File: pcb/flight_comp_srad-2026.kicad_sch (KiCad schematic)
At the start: 75 parts, among them J1 503398-1892, J2 Connector_3, J3 USB_B_Micro, J5 Vin_Bat, U1 IIM-20670, U3 RP2040, U4 ADXL375BCCZ-RL7, U5 MAX-M10M-00B, U6 W25Q128JVS, U7 XBP9B-DMSTB002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

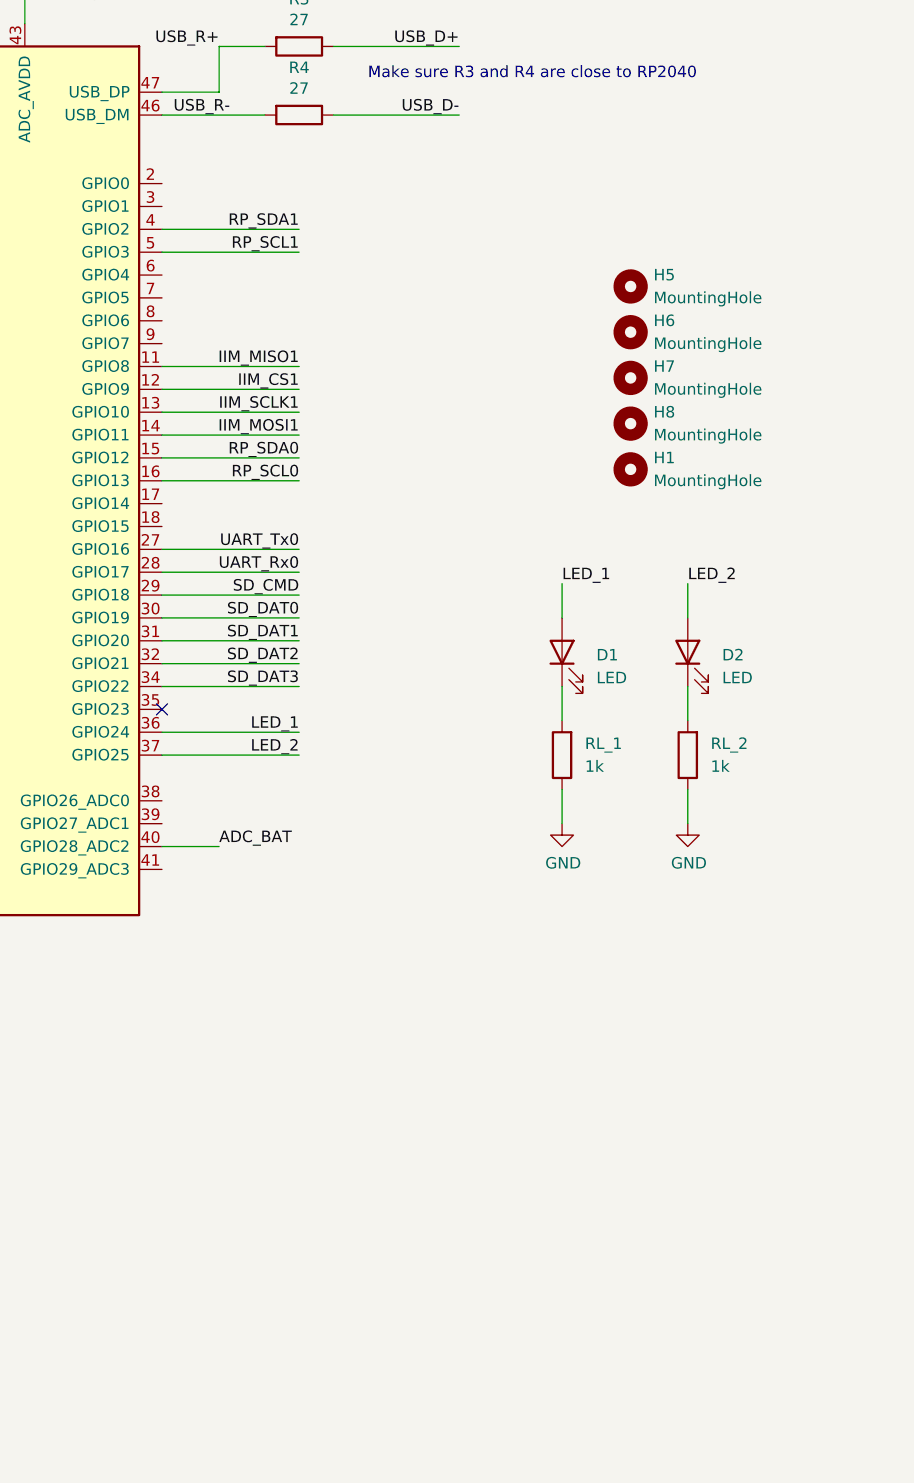
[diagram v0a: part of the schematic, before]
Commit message: Adición buzzer y corrección de algunos errores
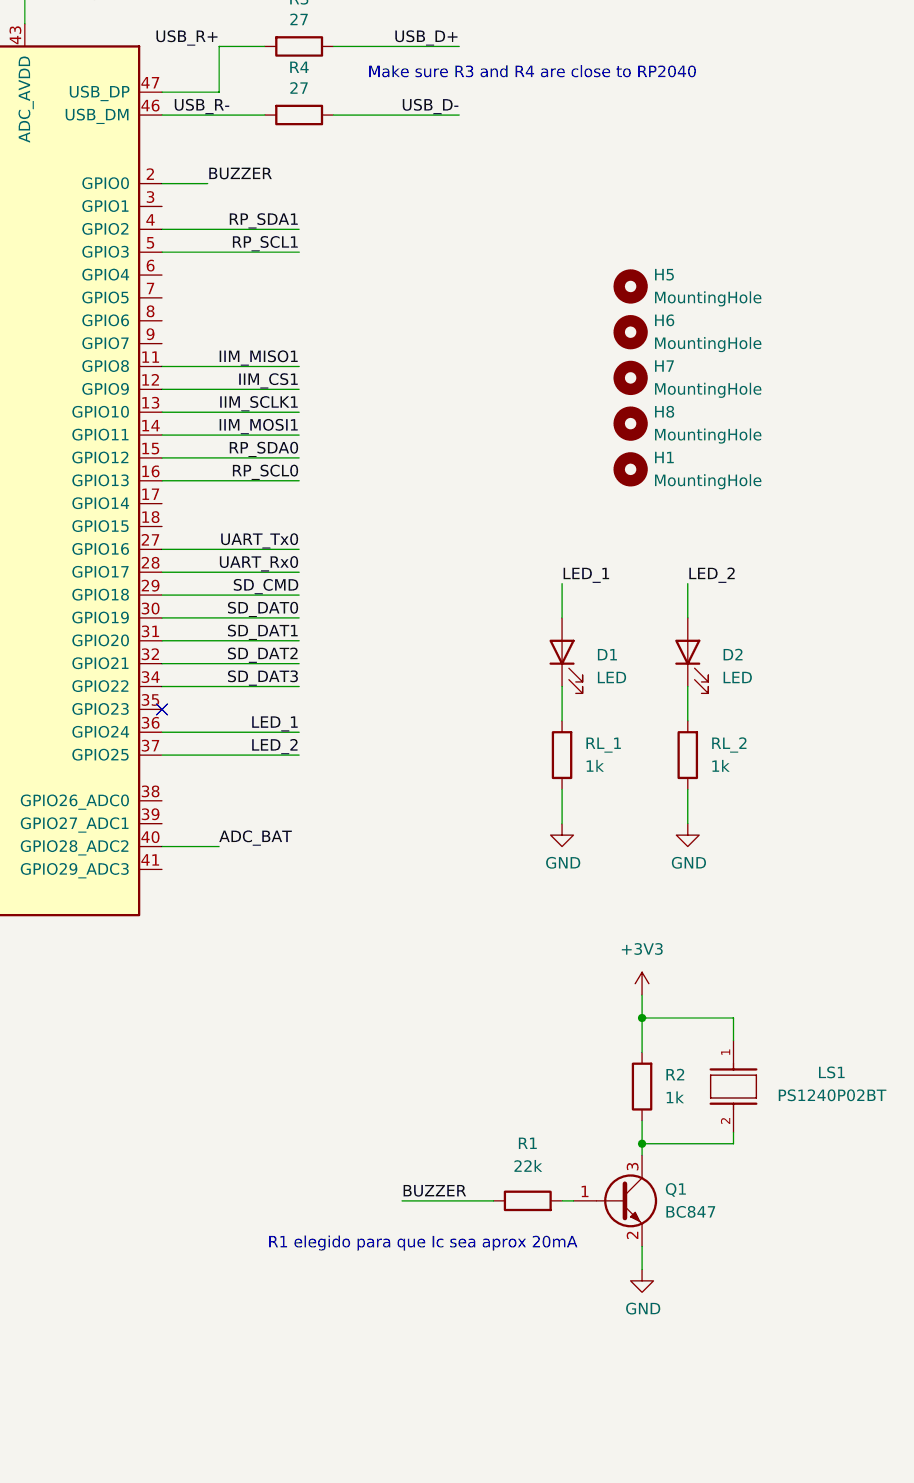
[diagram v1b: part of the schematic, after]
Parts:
- added LS1: PS1240P02BT, Buzzer_Beeper:Buzzer_TDK_PS1240P02BT_D12.2mm_H6.5mm, symbol PS1240P02BT:PS1240P02BT
- added Q1: BC847, Package_TO_SOT_SMD:SOT-23, symbol Transistor_BJT:BC847
- added R1: 22k, Resistor_SMD:R_0805_2012Metric, symbol Device:R
- added R2: 1k, Resistor_SMD:R_0805_2012Metric, symbol Device:R
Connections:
- net +3V3: now also LS1.1, R2.2
- net GND: now also Q1.2 (E)
- net BUZZER: now reaches U3.2 (GPIO0)
- net BUZZER: now also R1.1
- new net: Q1.1 (B), R1.2
- new net: LS1.2, Q1.3 (C), R2.1
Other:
- note added: "R1 elegido para que Ic sea aprox 20mA"

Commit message: quedan 5 errores
creo que todos los errores son inevitables por el diseño. quedan cosas tipo ancho del texto, pero debería salir bien todo lo importante en JLC
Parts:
- R3, R4: footprint Capacitor_SMD:C_0201_0603Metric -> Resistor_SMD:R_0603_1608Metric
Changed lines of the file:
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@@
 			)
 		)
-		(property "Footprint" "Capacitor_SMD:C_0201_0603Metric"
+		(property "Footprint" "Resistor_SMD:R_0603_1608Metric"
 			(at 500.38 151.892 90)
 			(effects
@@
 			)
 		)
-		(property "Footprint" "Capacitor_SMD:C_0201_0603Metric"
+		(property "Footprint" "Resistor_SMD:R_0603_1608Metric"
 			(at 500.38 159.512 90)
 			(effects
@@
 		(dnp no)
 		(fields_autoplaced yes)
-		(property "Reference" "#PWR034"
+		(property "Reference" "#PWR0101"
 			(at 538.48 262.89 0)
 			(effects
@@
 			(project "flight_comp_srad-2026"
 				(path "/142d7a80-3dfb-4605-bdd8-7dd9e7ca17c7"
-					(reference "#PWR034")
+					(reference "#PWR0101")
 					(unit 1)
 				)

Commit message: srad versión final ahora sí 2.0 intento 17
nigga
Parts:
- J2: footprint TCLib:PinHeader_1x03_P2.54mm_Vertical -> Connector_PinHeader_2.54mm:PinHeader_1x03_P2.54mm_Vertical
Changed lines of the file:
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@@
 			)
 		)
-		(property "Footprint" "TCLib:PinHeader_1x03_P2.54mm_Vertical"
+		(property "Footprint" "Connector_PinHeader_2.54mm:PinHeader_1x03_P2.54mm_Vertical"
 			(at 297.434 257.302 0)
 			(effects

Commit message: PARECE terminado
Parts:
- removed CGPS_3: 100n, Capacitor_SMD:C_0402_1005Metric, symbol Device:C
- added RSPI_1, RSPI_2, RSPI_3, RSPI_4: 1k, Resistor_SMD:R_0603_1608Metric, symbol Device:R
- added TP1, TP2: TestPoint, TestPoint:TestPoint_Pad_D1.0mm, symbol Connector:TestPoint
- CGPS_1: value 100n -> 1u; footprint Capacitor_SMD:C_0402_1005Metric -> Capacitor_SMD:C_0805_2012Metric
- CGPS_2: footprint Capacitor_SMD:C_0402_1005Metric -> Capacitor_SMD:C_0603_1608Metric
- CTX1, R8, RFLASH_1: now not fitted
- CXB_1, CXB_2: footprint Capacitor_SMD:C_0603_1608Metric -> Capacitor_SMD:C_0805_2012Metric
- D1: value LED -> LED_B
- D2: value LED -> LED_R
- RI2C_1, RI2C_2: value 10k -> 1k; footprint Resistor_SMD:R_0402_1005Metric -> Resistor_SMD:R_0603_1608Metric
- RI2C_3, RI2C_4: value 10k -> 1k; footprint Resistor_SMD:R_0805_2012Metric -> Resistor_SMD:R_0603_1608Metric
- RL_1: value 1k -> 39
- RL_2: value 1k -> 150
- U1: footprint Package_DFN_QFN:QFN-24-1EP_5x5mm_P0.65mm_EP3.25x3.25mm -> SRAD:QFN50P450X450X115-25N
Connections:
- net +3V3: now also RSPI_1.2, RSPI_2.2, RSPI_3.2, RSPI_4.2, TP1.1
- net GND: now also TP2.1
- net IIM_CS1: now also RSPI_4.1
- net IIM_MISO1: now also RSPI_1.1
- net IIM_MOSI1: now also RSPI_2.1
- net IIM_SCLK1: now also RSPI_3.1
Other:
- moved on the sheet: CIIM_1, CIIM_2, CIIM_3, CIIM_4, U1

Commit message: version final?
uwu
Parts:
- added TP3: TestPoint, TestPoint:TestPoint_Pad_D1.0mm, symbol Connector:TestPoint
- Div_res_bat1, Div_res_bat2: now not fitted
- RSPI_4: value 1k -> 10k
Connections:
- net +1V1: now also TP3.1
- no-connect marks 33 -> 43
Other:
- note added: "3V3?"
- moved on the sheet: TP2
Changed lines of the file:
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@@
 		)
 	)
+	(text "3V3?"
+		(exclude_from_sim no)
+		(at 144.272 61.722 0)
+		(effects
+			(font
+				(size 1.27 1.27)
+			)
+		)
+	)
 	(text "JLC04161H-7628E\nW=0.7\nGap=0.4\nThickness=0.4284 mm"
 		(exclude_from_sim no)
@@
 	)
 	(junction
+		(at 412.75 118.11)
+		(diameter 0)
+		(color 0 0 0 0)
+	)
+	(junction
 		(at 513.08 129.54)
 		(diameter 0)
@@
 	)
 	(no_connect
+		(at 485.14 186.69)
+	)
+	(no_connect
 		(at 48.26 50.8)
 	)
@@
 	)
 	(no_connect
+		(at 485.14 240.03)
+	)
+	(no_connect
+		(at 485.14 171.45)
+	)
+	(no_connect
 		(at 100.33 137.16)
 	)
 	(no_connect
+		(at 485.14 237.49)
+	)
+	(no_connect
 		(at 100.33 116.84)
 	)
@@
 	)
 	(no_connect
+		(at 485.14 184.15)
+	)
+	(no_connect
 		(at 306.07 130.81)
 	)
@@
 	)
 	(no_connect
+		(at 485.14 204.47)
+	)
+	(no_connect
 		(at 190.5 344.17)
 	)
@@
 	)
 	(no_connect
+		(at 485.14 179.07)
+	)
+	(no_connect
 		(at 190.5 331.47)
 	)
@@
 	)
 	(no_connect
+		(at 485.14 207.01)
+	)
+	(no_connect
+		(at 485.14 181.61)
+	)
+	(no_connect
 		(at 190.5 346.71)
 	)
@@
 		(at 190.5 361.95)
 	)
+	(no_connect
+		(at 485.14 245.11)
+	)
 	(wire
 		(pts
@@
 	(wire
 		(pts
-			(xy 485.14 168.91) (xy 490.22 168.91)
+			(xy 485.14 168.91) (xy 500.38 168.91)
 		)
 		(stroke
@@
 	(wire
 		(pts
+			(xy 412.75 115.57) (xy 412.75 118.11)
+		)
+		(stroke
+			(width 0)
+			(type default)
+		)
+	)
+	(wire
+		(pts
 			(xy 52.07 252.73) (xy 52.07 250.19)
 		)
@@
 	)
 	(label "BUZZER"
-		(at 490.22 168.91 0)
+		(at 500.38 168.91 180)
 		(effects
 			(font
 				(size 1.27 1.27)
 			)
-			(justify left bottom)
+			(justify right bottom)
 		)
 	)
@@
 			)
 		)
-		(property "Value" "1k"
+		(property "Value" "10k"
 			(at 52.832 330.454 90)
 			(effects
@@
 		(lib_name "GND_12")
 		(lib_id "power:GND")
-		(at 501.65 87.63 0)
+		(at 563.88 129.54 0)
 		(unit 1)
 		(exclude_from_sim no)
@@
 		(dnp no)
 		(property "Reference" "#PWR038"
-			(at 501.65 93.98 0)
+			(at 563.88 135.89 0)
 			(effects
 				(font
@@
 		)
 		(property "Value" "GND"
-			(at 501.777 92.0242 0)
+			(at 564.007 133.9342 0)
 			(effects
 				(font
@@
 		)
 		(property "Footprint" ""
-			(at 501.65 87.63 0)
+			(at 563.88 129.54 0)
 			(effects
 				(font
@@
 		)
 		(property "Datasheet" ""
-			(at 501.65 87.63 0)
+			(at 563.88 129.54 0)
 			(effects
 				(font
@@
 		)
 		(property "Description" ""
-			(at 501.65 87.63 0)
+			(at 563.88 129.54 0)
 			(effects
 				(font
@@
 		(in_bom yes)
 		(on_board yes)
-		(dnp no)
+		(dnp yes)
 		(property "Reference" "Div_res_bat2"
 			(at 76.2 72.39 0)
@@
 	(symbol
 		(lib_id "Connector:TestPoint")
-		(at 501.65 87.63 0)
+		(at 563.88 129.54 0)
 		(unit 1)
 		(exclude_from_sim no)
@@
 		(fields_autoplaced yes)
 		(property "Reference" "TP2"
-			(at 504.19 83.0579 0)
+			(at 566.42 124.9679 0)
 			(effects
 				(font
@@
 		)
 		(property "Value" "TestPoint"
-			(at 504.19 85.5979 0)
+			(at 566.42 127.5079 0)
 			(effects
 				(font
@@
 		)
 		(property "Footprint" "TestPoint:TestPoint_Pad_D1.0mm"
-			(at 506.73 87.63 0)
+			(at 568.96 129.54 0)
 			(effects
 				(font
@@
 		)
 		(property "Datasheet" "~"
-			(at 506.73 87.63 0)
+			(at 568.96 129.54 0)
 			(effects
 				(font
@@
 		)
 		(property "Description" "test point"
-			(at 501.65 87.63 0)
+			(at 563.88 129.54 0)
 			(effects
 				(font
@@
 	)
 	(symbol
+		(lib_id "Connector:TestPoint")
+		(at 412.75 115.57 0)
+		(unit 1)
+		(exclude_from_sim no)
+		(in_bom yes)
+		(on_board yes)
+		(dnp no)
+		(fields_autoplaced yes)
+		(property "Reference" "TP3"
+			(at 415.29 110.9979 0)
+			(effects
+				(font
+					(size 1.27 1.27)
+				)
+				(justify left)
+			)
+		)
+		(property "Value" "TestPoint"
+			(at 415.29 113.5379 0)
+			(effects
+				(font
+					(size 1.27 1.27)
+				)
+				(justify left)
+			)
+		)
+		(property "Footprint" "TestPoint:TestPoint_Pad_D1.0mm"
+			(at 417.83 115.57 0)
+			(effects
+				(font
+					(size 1.27 1.27)
+				)
+				(hide yes)
+			)
+		)
+		(property "Datasheet" "~"
+			(at 417.83 115.57 0)
+			(effects
+				(font
+					(size 1.27 1.27)
+				)
+				(hide yes)
+			)
+		)
+		(property "Description" "test point"
+			(at 412.75 115.57 0)
+			(effects
+				(font
+					(size 1.27 1.27)
+				)
+				(hide yes)
+			)
+		)
+		(pin "1"
+		)
+		(instances
+			(project "flight_comp_srad-2026"
+				(path "/142d7a80-3dfb-4605-bdd8-7dd9e7ca17c7"
+					(reference "TP3")
+					(unit 1)
+				)
+			)
+		)
+	)
+	(symbol
 		(lib_id "SRAD:MS561101BA03-50")
 		(at 290.83 130.81 0)
@@
 		(in_bom yes)
 		(on_board yes)
-		(dnp no)
+		(dnp yes)
 		(property "Reference" "Div_res_bat1"
 			(at 67.31 63.754 90)

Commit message: versión final ahora sí
OwO
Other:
- note removed: "I2C / SPI"
- note removed: "I2C / UART"
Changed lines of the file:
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@@
 		)
 	)
-	(text "I2C / UART"
+	(text "I2C"
 		(exclude_from_sim no)
 		(at 38.1 96.266 0)
@@
 		)
 	)
-	(text "I2C / SPI"
+	(text "I2C"
 		(exclude_from_sim no)
 		(at 265.684 98.298 0)

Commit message: https://drive.google.com/drive/folders/1AIpmniXnHx3TK0_vEmsLqZfZEH8VMv5M
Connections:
- net LED_1: now also U3.38 (GPIO26_ADC0); no longer U3.36 (GPIO24)
- net LED_2: now also U3.39 (GPIO27_ADC1); no longer U3.37 (GPIO25)
- net SD_CLK: now also U3.37 (GPIO25)
- no-connect marks 43 -> 41
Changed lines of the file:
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@@
 	)
 	(no_connect
-		(at 485.14 227.33)
-	)
-	(no_connect
 		(at 100.33 127)
 	)
 	(no_connect
-		(at 485.14 240.03)
-	)
-	(no_connect
 		(at 485.14 171.45)
 	)
@@
 	)
 	(no_connect
-		(at 485.14 237.49)
+		(at 485.14 229.87)
 	)
 	(no_connect
@@
 	)
 	(no_connect
+		(at 485.14 227.33)
+	)
+	(no_connect
 		(at 246.38 356.87)
 	)
@@
 	)
 	(no_connect
-		(at 485.14 181.61)
-	)
-	(no_connect
 		(at 190.5 346.71)
 	)
@@
 	(wire
 		(pts
+			(xy 485.14 237.49) (xy 500.38 237.49)
+		)
+		(stroke
+			(width 0)
+			(type default)
+		)
+	)
+	(wire
+		(pts
 			(xy 74.93 38.1) (xy 81.28 38.1)
 		)
@@
 	(wire
 		(pts
-			(xy 485.14 242.57) (xy 491.49 242.57)
+			(xy 485.14 242.57) (xy 500.38 242.57)
 		)
 		(stroke
@@
 	(wire
 		(pts
+			(xy 485.14 240.03) (xy 500.38 240.03)
+		)
+		(stroke
+			(width 0)
+			(type default)
+		)
+	)
+	(wire
+		(pts
 			(xy 261.62 57.15) (xy 278.13 57.15)
 		)
@@
 	(wire
 		(pts
-			(xy 485.14 229.87) (xy 500.38 229.87)
-		)
-		(stroke
-			(width 0)
-			(type default)
-		)
-	)
-	(wire
-		(pts
 			(xy 485.14 212.09) (xy 500.38 212.09)
 		)
@@
 	)
 	(label "ADC_BAT"
-		(at 491.49 242.57 0)
+		(at 500.38 242.57 180)
 		(effects
 			(font
 				(size 1.27 1.27)
 			)
-			(justify left bottom)
+			(justify right bottom)
 		)
 	)
@@
 		)
 	)
+	(label "LED_1"
+		(at 500.38 237.49 180)
+		(effects
+			(font
+				(size 1.27 1.27)
+			)
+			(justify right bottom)
+		)
+	)
 	(label "QSPI_SD2"
 		(at 407.67 179.07 0)
@@
 	)
 	(label "LED_2"
-		(at 500.38 232.41 180)
+		(at 500.38 240.03 180)
 		(effects
 			(font
@@
 		)
 	)
-	(label "LED_1"
-		(at 500.38 229.87 180)
+	(label "RUN"
+		(at 407.67 222.25 0)
 		(effects
 			(font
 				(size 1.27 1.27)
 			)
-			(justify right bottom)
+			(justify left bottom)
 		)
 	)
-	(label "RUN"
-		(at 407.67 222.25 0)
+	(label "SD_DAT0"
+		(at 243.84 124.46 180)
 		(effects
 			(font
 				(size 1.27 1.27)
 			)
-			(justify left bottom)
+			(justify right bottom)
 		)
 	)
-	(label "SD_DAT0"
-		(at 243.84 124.46 180)
+	(label "SD_CLK"
+		(at 500.38 232.41 180)
 		(effects
 			(font

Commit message: xbee driver
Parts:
- LS1: DESCRIPTION Buzzers Transducer, Externally Driven Piezo 3V 4kHz 60dB @ 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 -> (none)
